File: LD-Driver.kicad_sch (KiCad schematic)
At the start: 3 parts, among them J1 BASYS3, U1 MCP4728

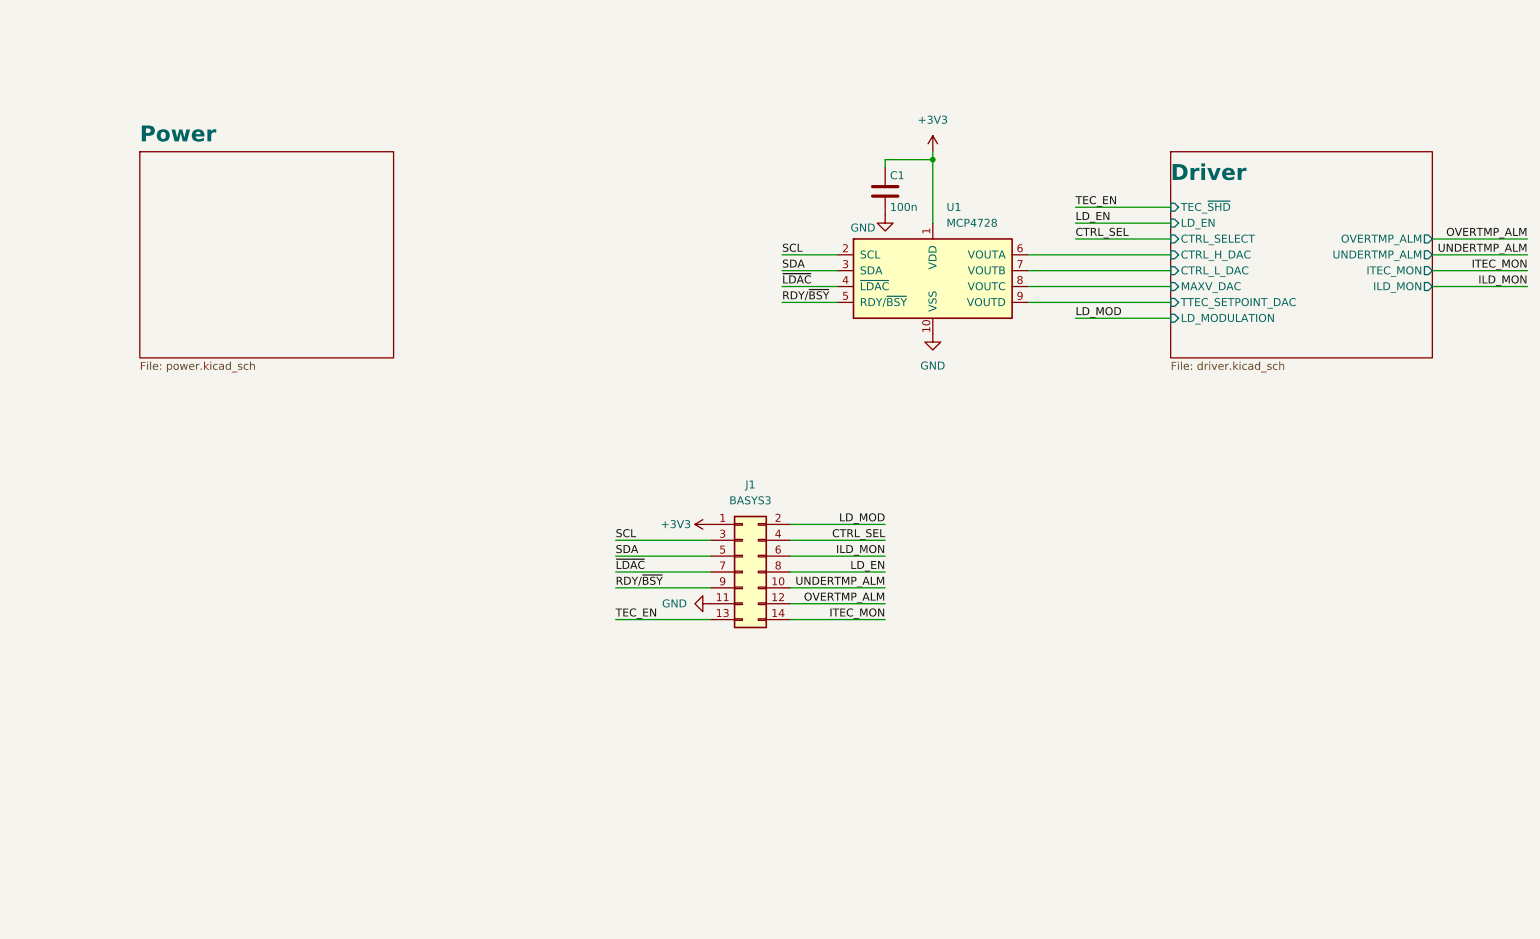
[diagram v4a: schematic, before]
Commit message: fix: shorted PVDD and VDD on MIC
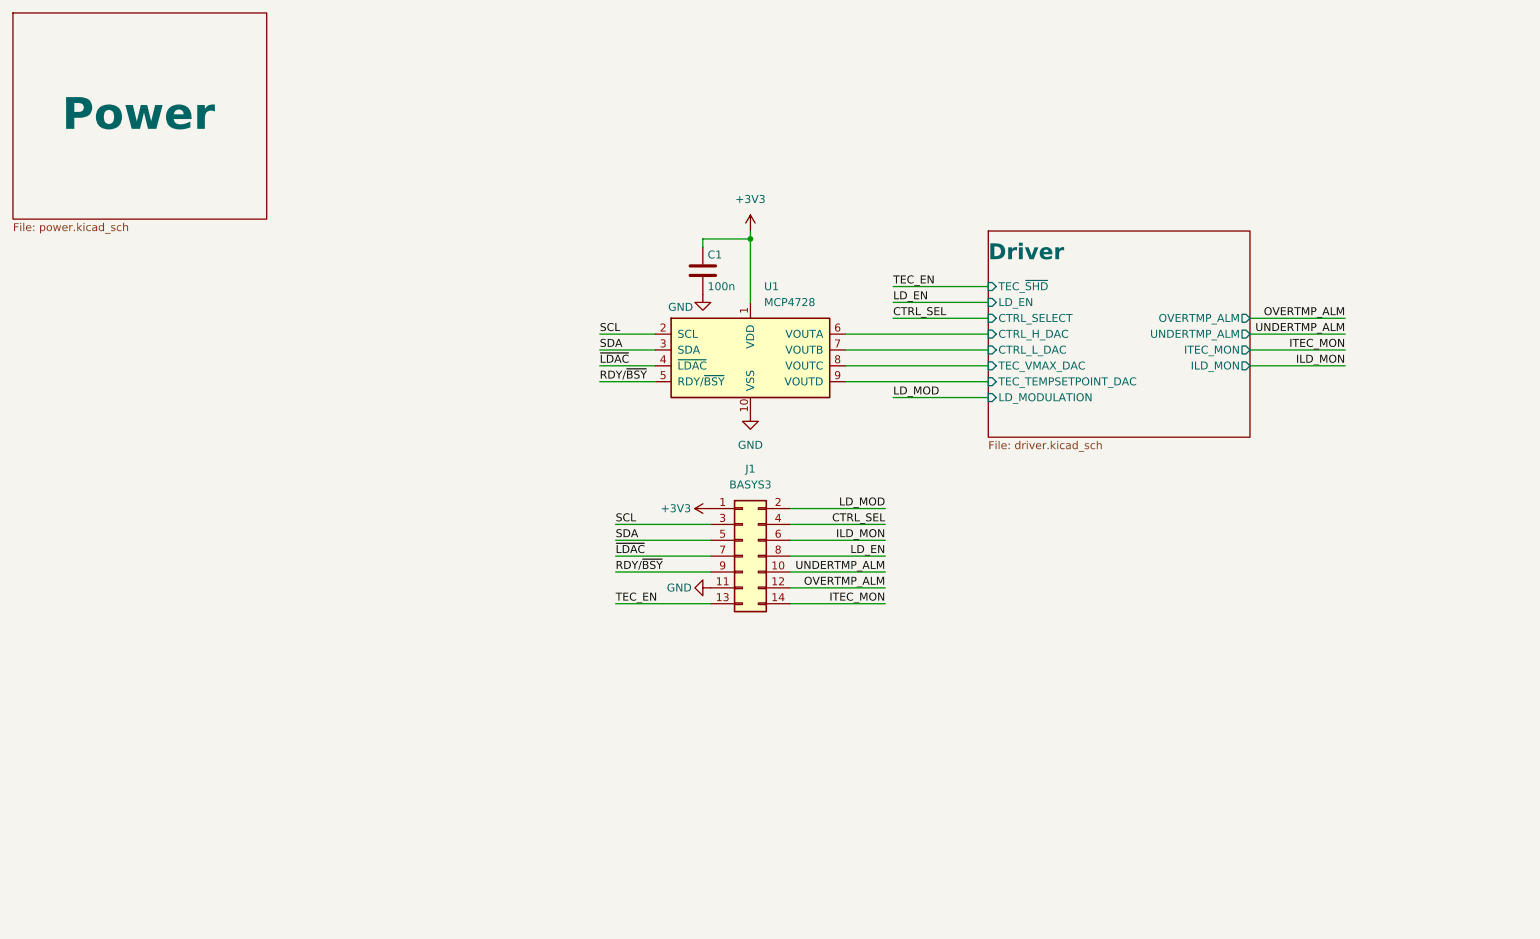
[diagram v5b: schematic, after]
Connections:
- net Driver/MAXV_DAC renamed Driver/TEC_VMAX_DAC
- net Driver/TTEC_SETPOINT_DAC renamed Driver/TEC_TEMPSETPOINT_DAC
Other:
- sheet Driver ports: added TEC_TEMPSETPOINT_DAC, TEC_VMAX_DAC; removed MAXV_DAC, TTEC_SETPOINT_DAC
- moved on the sheet: C1, J1, U1
